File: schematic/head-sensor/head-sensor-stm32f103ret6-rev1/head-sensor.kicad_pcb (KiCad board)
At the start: 2 copper layers, 48 parts, among them P1 MICROSD-SDIO-CD, P10 SensorsIn, P11 USART1, P12 SensorsGND, P13 RFID-RC522-MODULE, P14 NRF24L01, P15 HeadLEDs, P2 Vibroengines, P3 NRST, P4 SWGND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

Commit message: Some pcb routing
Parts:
- moved R6 141.8 mm to (161.9, 129.3)
- moved P2 139.3 mm to (123.1, 119.0)
- moved P15 136.2 mm to (154.3, 115.2)
- moved P14 135.3 mm to (134.9, 96.5), turned to 90 degrees
- moved R7 130.7 mm to (144.0, 121.3)
- moved Q8 122.8 mm to (133.0, 126.5)
- moved P6 117.4 mm to (122.4, 104.9)
- moved P13 117.4 mm to (120.9, 73.9), turned to 270 degrees
- moved Q9 113.6 mm to (128.8, 100.8), turned to 180 degrees
- moved P11 111.7 mm to (143.5, 85.3), turned to 180 degrees
- moved Q7 110.5 mm to (123.2, 111.5)
- moved Q1 110.0 mm to (131.1, 105.7), turned to 270 degrees
- moved C7 103.9 mm to (129.0, 97.8), turned to 180 degrees
- moved R2 101.7 mm to (133.1, 71.9), turned to 270 degrees
- moved R8 99.0 mm to (142.9, 117.5), turned to 180 degrees
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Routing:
- net N-0000033: track 0.00 -> 43.0 mm, vias 0 -> 2
- net N-0000034: track 0.00 -> 42.7 mm, vias 0 -> 2
- net AGND: track 0.00 -> 41.5 mm, vias 0 -> 5
- net N-000008: track 0.00 -> 41.4 mm
- net N-0000049: track 0.00 -> 41.2 mm
- net +3.3V: track 0.00 -> 40.3 mm
- net N-000007: track 0.00 -> 39.4 mm
- net N-0000035: track 0.00 -> 34.6 mm
- net N-0000032: track 0.00 -> 27.3 mm
- net N-0000019: track 0.00 -> 22.6 mm
- net N-0000045: track 0.00 -> 19.4 mm
- net N-0000020: track 0.00 -> 17.4 mm
- net N-0000046: track 0.00 -> 16.0 mm
- net N-0000047: track 0.00 -> 13.6 mm
- net N-0000057: track 0.00 -> 13.4 mm
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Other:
- net class Default: clearance 0.254 -> 0.195; trace_width 0.254 -> 0.3; via_dia 0.889 -> 1.5; via_drill 0.635 -> 1
- rule trace_clearance: 0.254 -> 0.195

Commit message: Head sensor pcb
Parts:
- moved R6 57.6 mm to (111.3, 101.9), turned to 270 degrees
- moved P2 44.7 mm to (82.3, 100.7), turned to 270 degrees
- moved Q1 44.0 mm to (87.1, 107.1)
- moved Q2 37.2 mm to (87.1, 103.5), turned to 270 degrees
- moved P15 35.2 mm to (120.0, 107.2), turned to 180 degrees
- moved R7 32.6 mm to (117.9, 101.9), turned to 270 degrees
- moved Q8 31.6 mm to (114.6, 100.8), turned to 90 degrees
- moved R8 23.7 mm to (125.1, 101.9), turned to 270 degrees
- moved Q7 18.4 mm to (108.2, 100.8), turned to 90 degrees
- moved Q5 15.6 mm to (87.1, 92.5), turned to 270 degrees
- moved Q4 11.2 mm to (87.1, 96.1), turned to 270 degrees
- moved P6 10.7 mm to (133.1, 104.6)
- moved Q3 10.6 mm to (87.1, 99.8), turned to 270 degrees
- moved Q6 9.94 mm to (87.1, 88.9), turned to 270 degrees
- moved Q9 6.86 mm to (121.9, 100.7), turned to 90 degrees
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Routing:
- net +3.3V: track 40.3 -> 86.4 mm
- net N-0000042: track 0.00 -> 31.4 mm
- net N-0000041: track 0.00 -> 29.1 mm
- net AGND: track 41.5 -> 67.0 mm, vias 5 -> 7
- net N-0000043: track 0.00 -> 19.5 mm
- net N-0000027: track 0.00 -> 16.1 mm
- net N-0000023: track 0.00 -> 13.9 mm
- net N-0000044: track 0.00 -> 13.8 mm
- net N-0000025: track 4.05 -> 8.89 mm

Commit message: head sensor pcb near no be done
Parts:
- added P16: Power, PIN_ARRAY_2X1, B.Cu at (97.5, 82.0)
- moved P9 107.6 mm to (147.6, 107.2)
- moved P3 63.1 mm to (109.2, 89.2)
- moved P12 57.4 mm to (101.9, 67.4), turned to 180 degrees
- moved C1 53.1 mm to (101.3, 73.7), turned to 270 degrees
- moved P5 48.4 mm to (91.2, 77.5), turned to 90 degrees
- moved C3 44.6 mm to (105.9, 73.7), turned to 270 degrees
- moved P4 44.2 mm to (97.5, 77.0)
- moved U1 11.3 mm to (103.9, 84.3)
- moved C4 9.20 mm to (111.0, 81.5)
- moved C5 8.86 mm to (111.0, 86.6)
- moved P2 8.64 mm to (90.9, 100.6)
- moved Q1 7.87 mm to (95.0, 107.1)
- moved Q2 7.87 mm to (95.0, 103.5)
- moved Q3 7.87 mm to (95.0, 99.8)
- moved Q4 7.87 mm to (95.0, 96.1)
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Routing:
- net AGND: track 67.0 -> 153.9 mm, vias 7 -> 12
- net N-0000038: track 0.00 -> 28.2 mm
- net N-0000041: track 0.00 -> 26.8 mm
- net N-0000039: track 0.00 -> 26.6 mm
- net +BATT: track 0.00 -> 25.8 mm, vias 0 -> 1
- net N-0000040: track 0.00 -> 24.9 mm
- net +3.3V: track 86.4 -> 108.9 mm
- net N-0000031: track 8.02 -> 24.9 mm
- net N-0000045: track 0.00 -> 11.3 mm, vias 0 -> 2
- net N-0000053: track 0.00 -> 11.2 mm
- net N-000004: track 0.00 -> 9.91 mm
- net N-0000029: track 0.00 -> 9.81 mm
- net N-0000016: track 0.00 -> 7.79 mm
- net N-0000054: track 0.00 -> 7.51 mm
- net N-000003: track 0.00 -> 6.69 mm
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
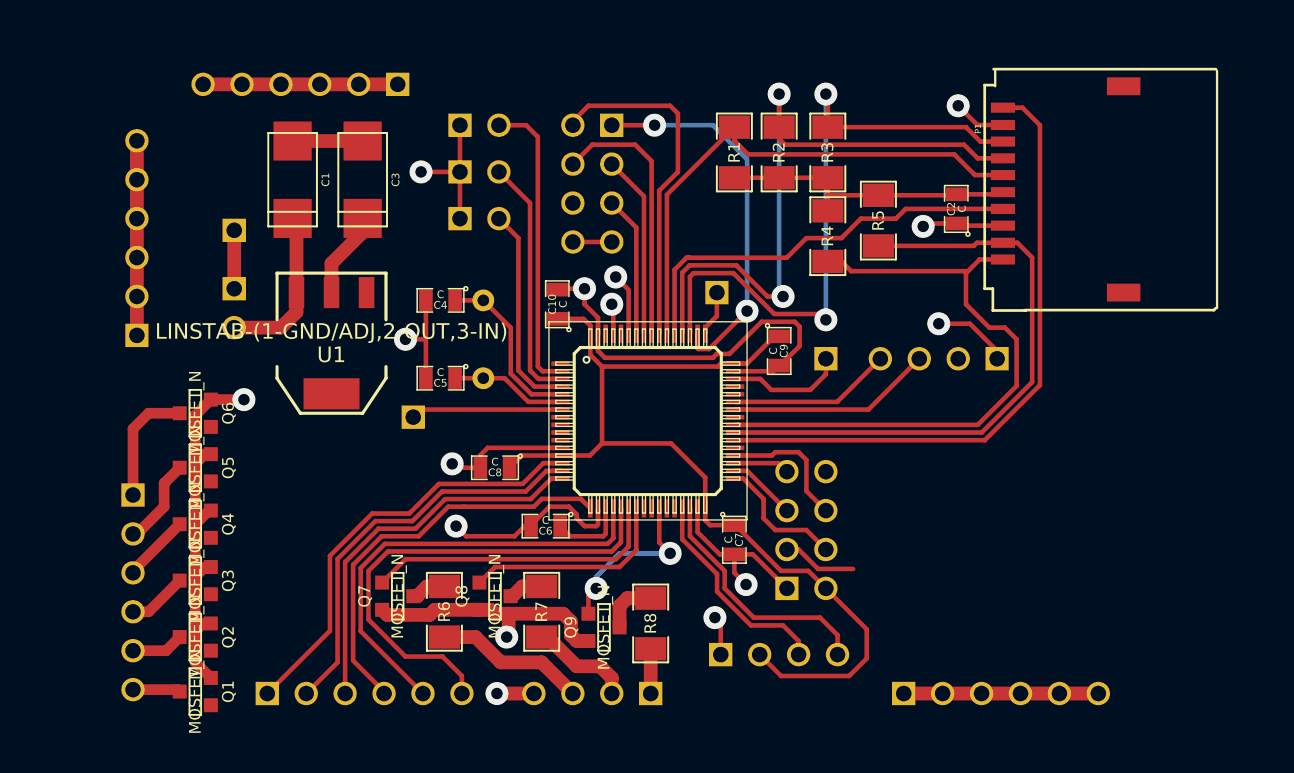
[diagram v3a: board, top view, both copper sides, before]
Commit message: Head sensor pcb done
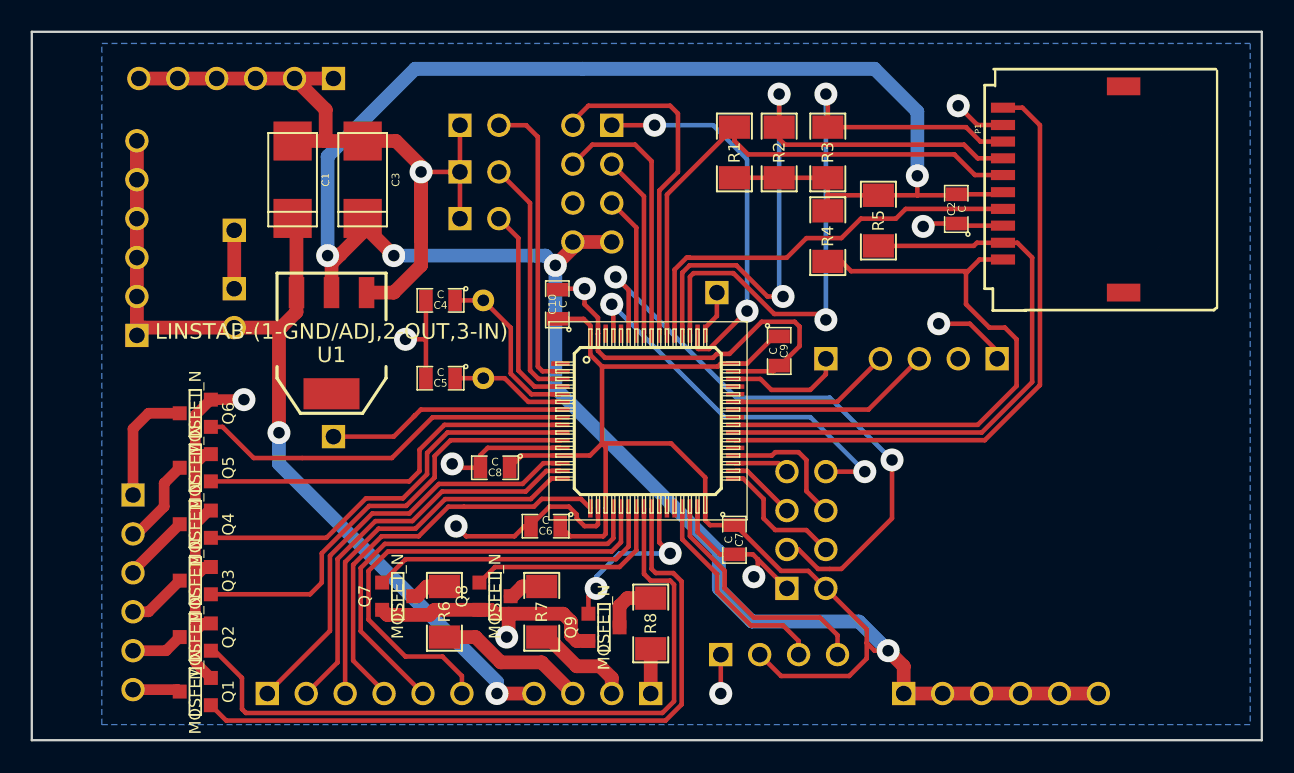
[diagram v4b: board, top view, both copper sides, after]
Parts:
- moved P3 5.36 mm to (104.0, 90.4)
- moved P12 4.21 mm to (97.7, 67.1)
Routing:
- net +3.3V: track 108.9 -> 227.2 mm, vias 0 -> 5
- net N-0000012: track 0.00 -> 47.6 mm
- net N-0000020: track 0.00 -> 45.8 mm
- net +BATT: track 25.8 -> 62.1 mm, vias 1 -> 2
- net N-0000027: track 8.89 -> 39.6 mm, vias 1 -> 2
- net N-0000013: track 0.00 -> 28.9 mm
- net N-0000011: track 0.00 -> 26.5 mm
- net N-0000014: track 0.00 -> 25.2 mm
- net N-0000015: track 0.00 -> 24.8 mm
- net AGND: track 153.9 -> 177.6 mm
- net N-0000028: track 1.96 -> 25.5 mm, vias 1 -> 2
- net N-0000029: track 9.81 -> 15.7 mm
- added copper zone on B.Cu, net AGND
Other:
- board outline added: 80.3 x 46.2 mm

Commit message: FW: SPI manager implemented, nrf24l01 device beginned, need input listener or some other object. HW: 3.5 terminals now used
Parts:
- P10, P12, P2, P5, P9: footprint PIN_ARRAY-6X1 -> TERMINALS_6
- P16: footprint PIN_ARRAY_2X1 -> TERMINALS_2
- moved Q1 4.57 mm to (90.4, 107.1)
- moved Q2 4.57 mm to (90.4, 103.5)
- moved Q3 4.57 mm to (90.4, 99.8)
- moved Q4 4.57 mm to (90.4, 96.1)
- moved Q5 4.57 mm to (90.4, 92.5)
- moved Q6 4.57 mm to (90.4, 88.9)
- moved P12 4.47 mm to (102.1, 66.5), turned to 0 degrees
- moved P5 4.20 mm to (87.4, 75.7)
- moved P2 4.10 mm to (87.4, 98.6)
- moved P9 3.84 mm to (151.4, 106.7)
- moved P10 2.96 mm to (103.1, 106.7)
- moved P16 0.76 mm to (97.5, 82.8)
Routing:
- net AGND: track 177.6 -> 194.3 mm
- net +BATT: track 62.1 -> 75.8 mm
- net N-0000016: track 7.79 -> 2.40 mm
- net N-0000011: track 26.5 -> 31.0 mm
- net N-0000020: track 45.8 -> 50.4 mm
- net N-0000014: track 25.2 -> 29.7 mm
- net N-0000015: track 24.8 -> 29.3 mm
- net N-0000012: track 47.6 -> 52.0 mm
- net N-0000038: track 28.2 -> 32.1 mm
- net N-0000013: track 28.9 -> 32.4 mm
- net N-0000019: track 5.73 -> 2.37 mm
- net +3.3V: track 227.2 -> 230.5 mm
- net N-0000018: track 4.44 -> 2.30 mm
- net N-0000017: track 3.89 -> 2.22 mm
- net N-0000039: track 26.6 -> 27.9 mm
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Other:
- board size 80.3 x 46.2 mm -> 81.8 x 46.2 mm
- net class Default: trace_width 0.3 -> 0.9
